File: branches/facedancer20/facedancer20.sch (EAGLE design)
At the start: 20 parts, among them CN1 HOST, CN2 TARGET, CN3 USB-A-S, Q1 12MHz, U1 F261X---PM64, U2 FT232RL-BASICSSOP, U4 MAX3421ESMD

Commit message: FD20 ready for first test run.
git-svn-id: https://svn.code.sf.net/p/goodfet/code@1346 12e2690d-a6be-4b82-a7b7-67c4a43b65c8
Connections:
- removed net N$9: U4.GPX
- new net GPX: U1.43, U4.GPX
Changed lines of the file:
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@@
 </segment>
 </net>
-<net name="N$9" class="0">
+<net name="GPX" class="0">
 <segment>
 <pinref part="U4" gate="G$1" pin="GPX"/>
@@
 <label x="200.66" y="43.18" size="1.778" layer="95"/>
 </segment>
+<segment>
+<pinref part="U1" gate="G$1" pin="43"/>
+<wire x1="127" y1="55.88" x2="134.62" y2="55.88" width="0.1524" layer="91"/>
+<label x="129.54" y="55.88" size="1.778" layer="95"/>
+</segment>
 </net>

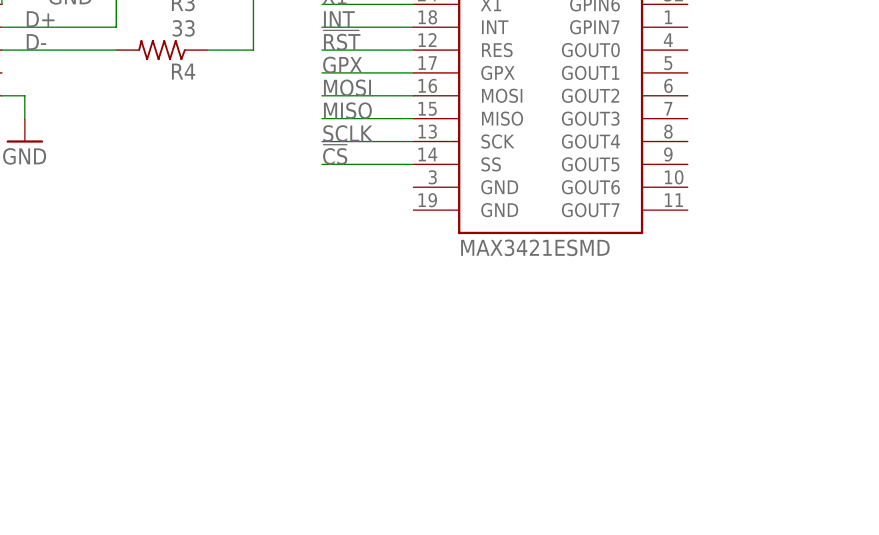
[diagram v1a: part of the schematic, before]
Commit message: Added erratum note to FD20 schematic.
git-svn-id: https://svn.code.sf.net/p/goodfet/code@1387 12e2690d-a6be-4b82-a7b7-67c4a43b65c8
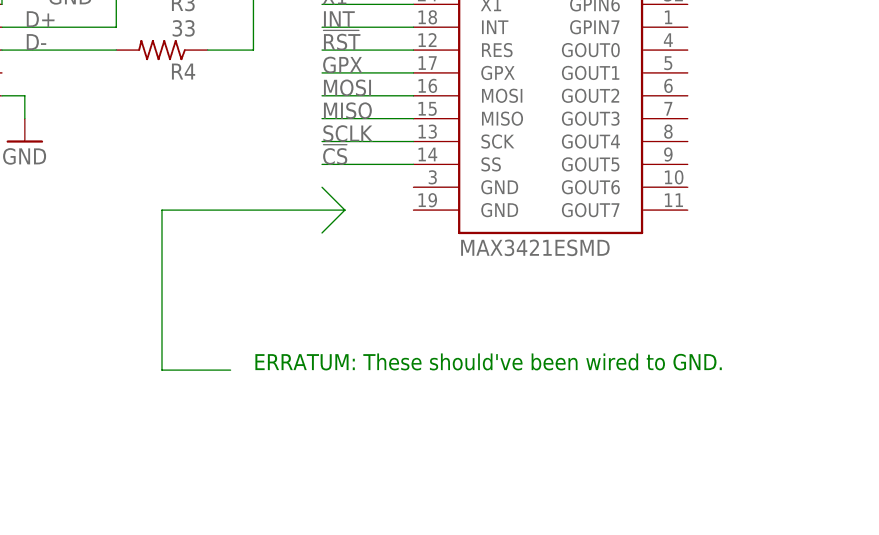
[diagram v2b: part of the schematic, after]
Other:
- note added: "ERRATUM: These should've been wired to GND."
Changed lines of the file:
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@@
 <text x="0" y="7.62" size="1.778" layer="91">Facedancer20</text>
 <text x="0" y="5.08" size="1.778" layer="91">A GoodFET for Exploiting USB</text>
+<text x="193.04" y="10.16" size="1.778" layer="91">ERRATUM: These should've been wired to GND.</text>
 </plain>
 <instances>
@@
 </segment>
 </net>
+<net name="N$3" class="0">
+<segment>
+<wire x1="190.5" y1="10.16" x2="182.88" y2="10.16" width="0.1524" layer="91"/>
+<wire x1="182.88" y1="10.16" x2="182.88" y2="27.94" width="0.1524" layer="91"/>
+<wire x1="182.88" y1="27.94" x2="203.2" y2="27.94" width="0.1524" layer="91"/>
+<wire x1="200.66" y1="30.48" x2="203.2" y2="27.94" width="0.1524" layer="91"/>
+<wire x1="203.2" y1="27.94" x2="200.66" y2="25.4" width="0.1524" layer="91"/>
+</segment>
+</net>
